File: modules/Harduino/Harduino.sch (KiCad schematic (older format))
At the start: 30 parts, among them J1 2, J10 11, J11 12, J12 13, J13 A0, J14 A1, J15 A2, J16 A3, J17 A4, J18 A5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

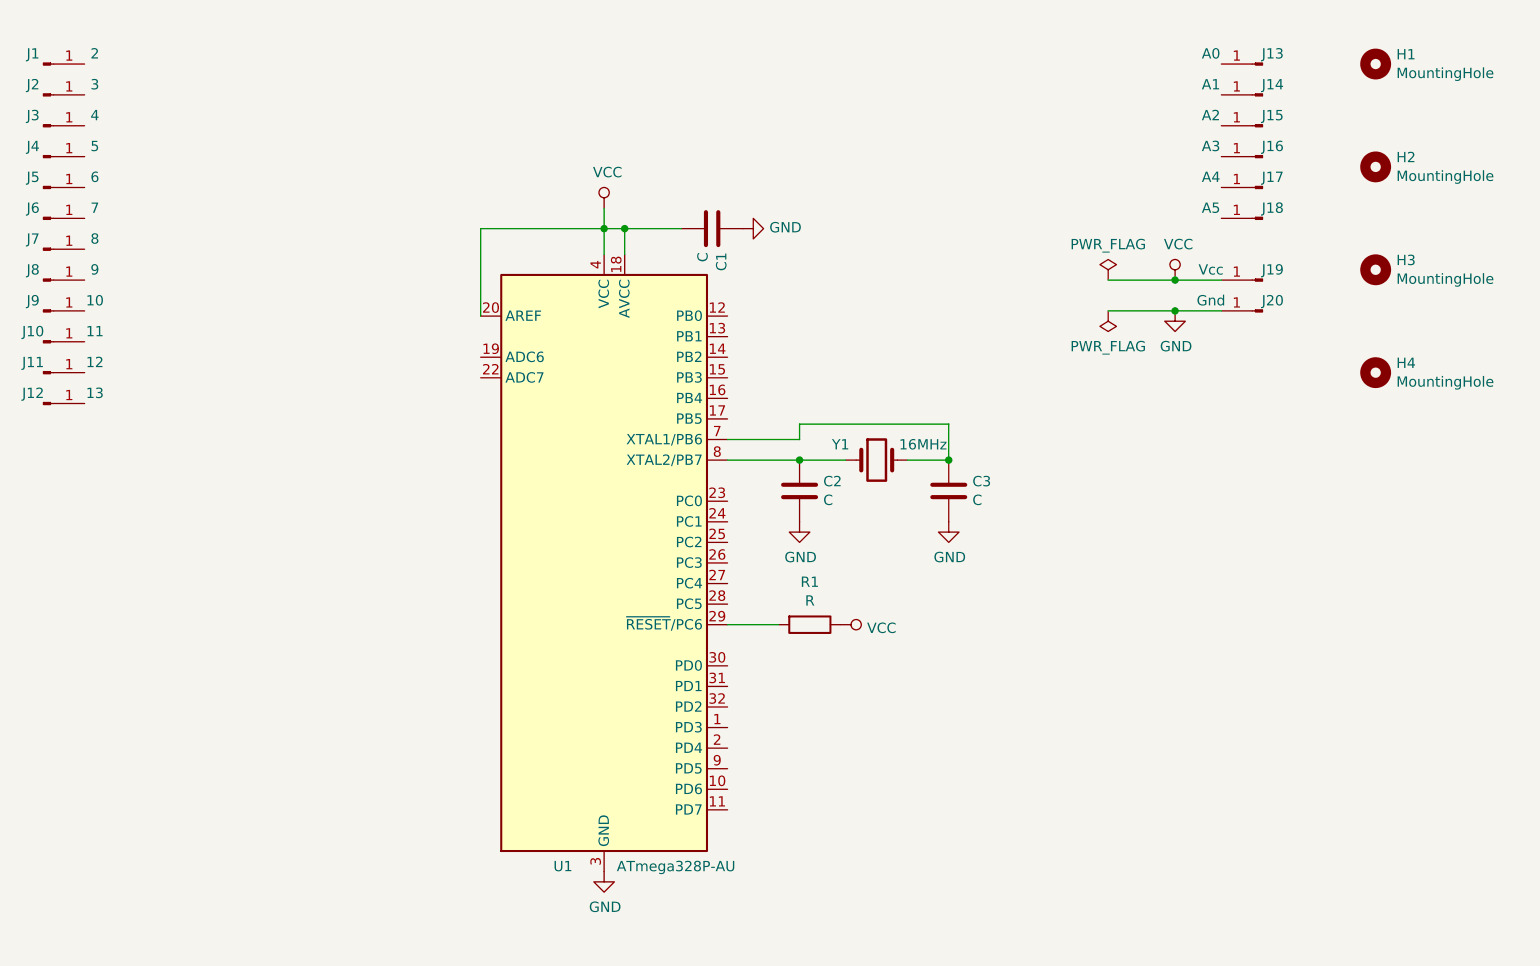
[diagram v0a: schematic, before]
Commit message: Connect AVR to pins
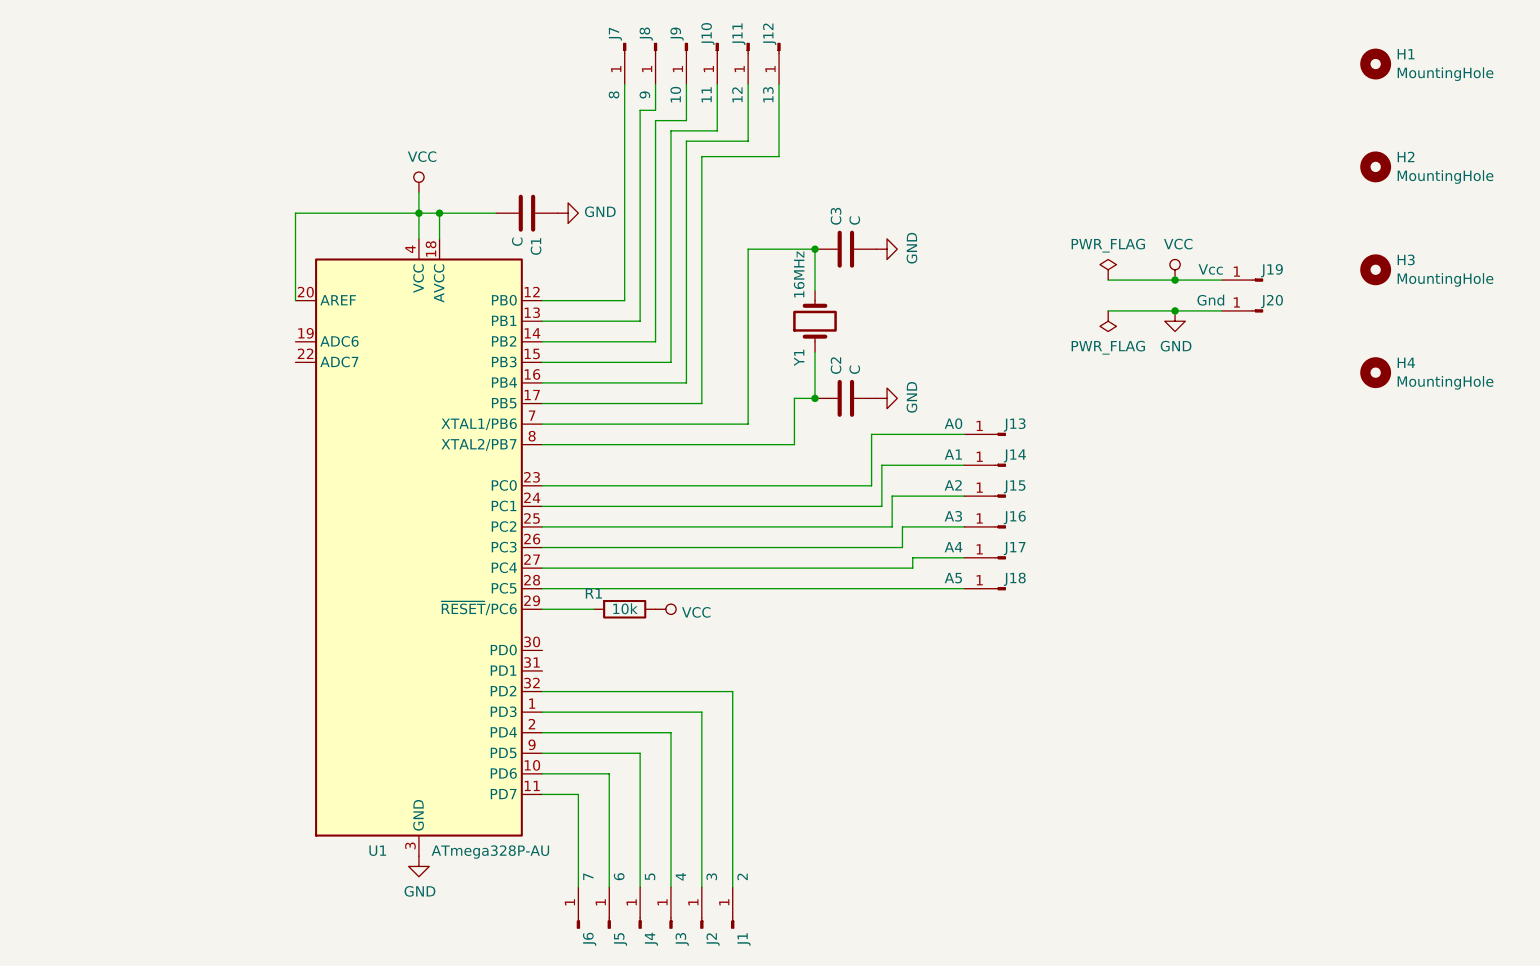
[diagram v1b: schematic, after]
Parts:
- R1: value R -> 10k
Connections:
- net at J1.1 (Pin_1): now also U1.32 (PD2)
- net at J2.1 (Pin_1): now also U1.1 (PD3)
- net at J3.1 (Pin_1): now also U1.2 (PD4)
- net at J4.1 (Pin_1): now also U1.9 (PD5)
- net at J5.1 (Pin_1): now also U1.10 (PD6)
- net at J6.1 (Pin_1): now also U1.11 (PD7)
- net at J7.1 (Pin_1): now also U1.12 (PB0)
- net at J8.1 (Pin_1): now also U1.13 (PB1)
- net at J9.1 (Pin_1): now also U1.14 (PB2)
- net at J10.1 (Pin_1): now also U1.15 (PB3)
- net at J11.1 (Pin_1): now also U1.16 (PB4)
- net at J13.1 (Pin_1): now also U1.23 (PC0)
- net at J14.1 (Pin_1): now also U1.24 (PC1)
- net at J15.1 (Pin_1): now also U1.25 (PC2)
- net at J16.1 (Pin_1): now also U1.26 (PC3)
- net at J17.1 (Pin_1): now also U1.27 (PC4)
- net at J18.1 (Pin_1): now also U1.28 (PC5)
- net at J12.1 (Pin_1): now also U1.17 (PB5)
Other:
- moved on the sheet: C1, C2, C3, J1, J10, J11, J12, J13, J14, J15, J16, J17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

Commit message: Place AVR in PCB
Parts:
- U1: symbol MCU_Microchip_ATmega:ATmega328P-AU -> Harduino-rescue:ATmega328P-AU-MCU_Microchip_ATmega
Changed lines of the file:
@@
 $EndComp
 $Comp
-L MCU_Microchip_ATmega:ATmega328P-AU U1
+L Harduino-rescue:ATmega328P-AU-MCU_Microchip_ATmega U1
 U 1 1 5D8CAD7F
 P 2850 4850
